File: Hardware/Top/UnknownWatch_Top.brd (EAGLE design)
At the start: 38 x 38 mm, 54 parts, among them SW1 SWITCH.MOM, SW6 SWITCH.MOM, U2 NRF52832_MODULE_MDBT42, U4 PCF8523, U5 PHOTOTRANSISTOR

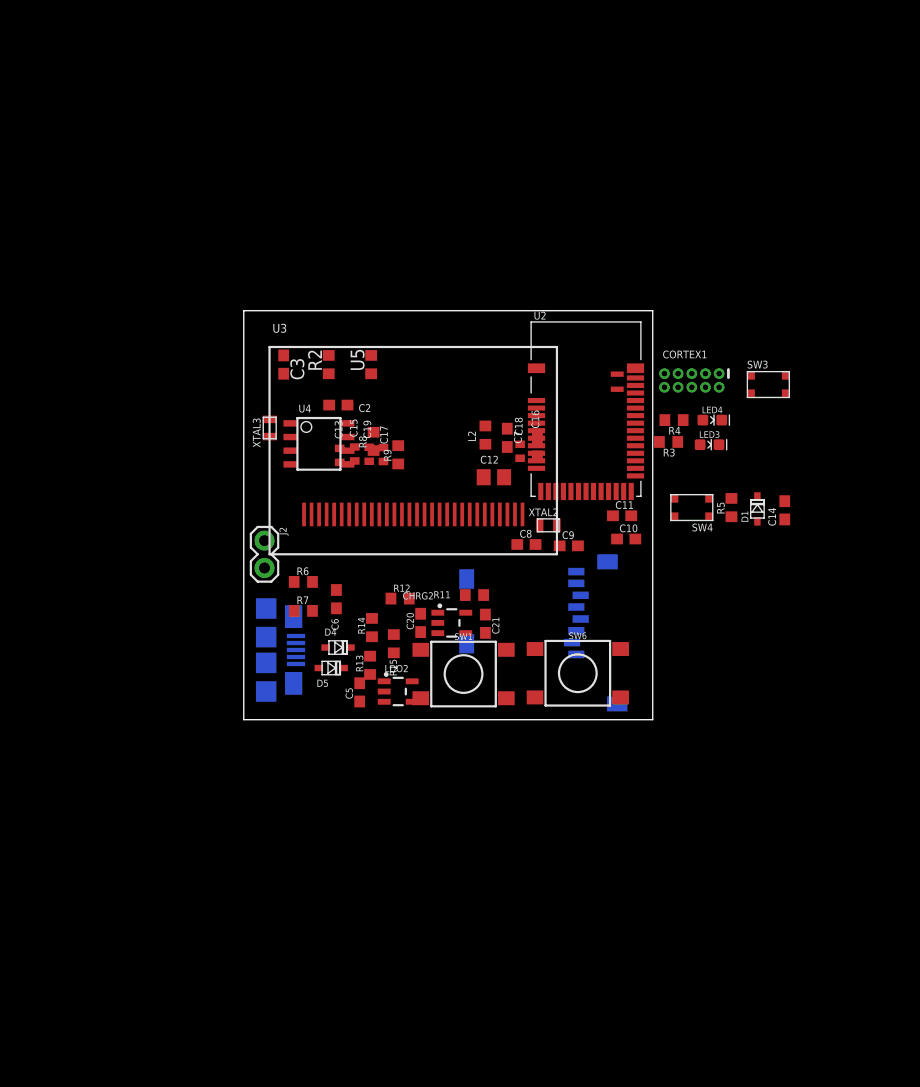
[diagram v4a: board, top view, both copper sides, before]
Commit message: Added connections from bottom to top board and other various changes.
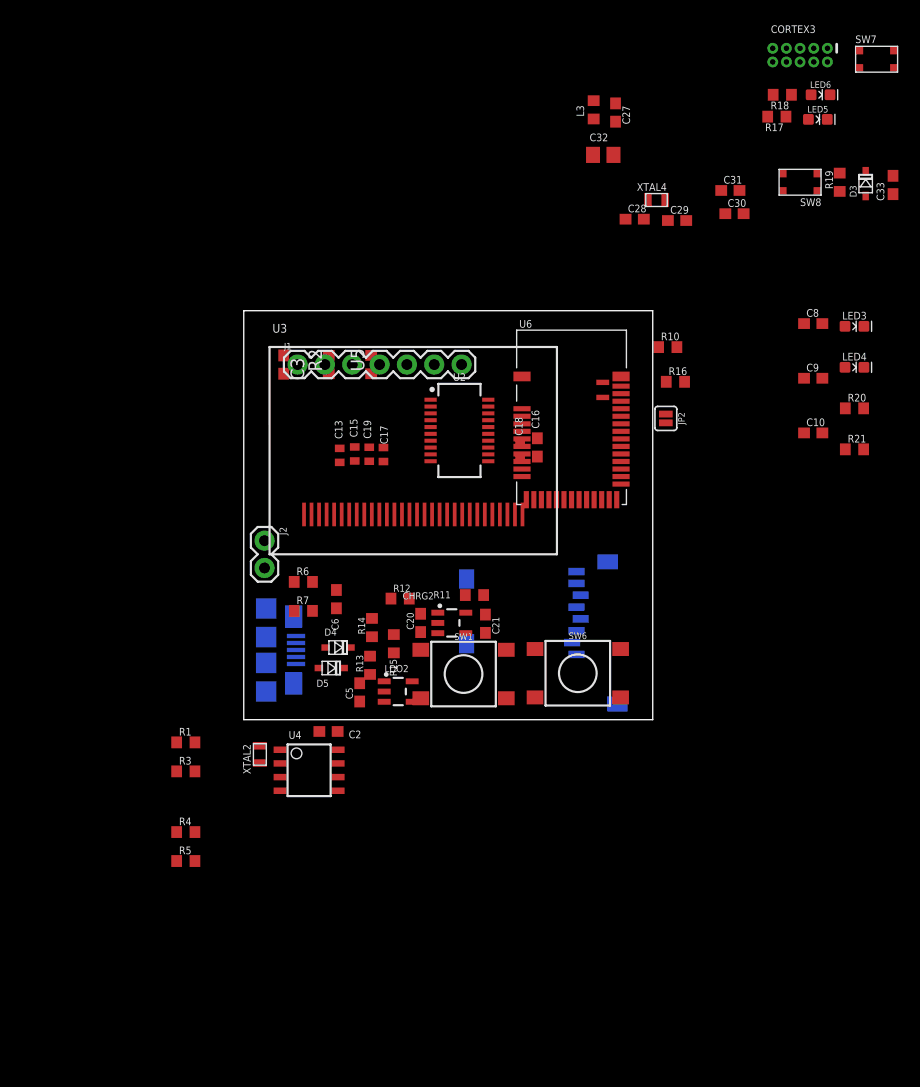
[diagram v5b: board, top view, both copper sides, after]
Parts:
- removed C11: 300p, LinnesLab-Passives:C0603
- removed C12: 10u, LinnesLab-Passives:C0805
- removed C14: 100n, LinnesLab-Passives:C0603
- removed C7: 1u, LinnesLab-Passives:C0603
- removed CORTEX1: CORTEX_DEBUG_PTH, LinnesLab-Connectors:2X5-PTH-1.27MM
- removed D1: (no value), LinnesLab-DiscreteSemi:USC
- removed L2: 10u, LinnesLab-Passives:L0603
- removed R8, R9: 10k, LinnesLab-Passives:R0603
- removed SW3, SW4: (no value), LinnesLab-Switches:BUTTON-GULLWING
- removed XTAL3: 32.7680kHz, LinnesLab-Clocks:2-SMD.NOLEAD.2.0MMTO1.2MM
- added C27: 1u, LinnesLab-Passives:C0603
- added C28, C29: (no value), LinnesLab-Passives:C0603
- added C30, C31: 300p, LinnesLab-Passives:C0603
- added C32: 10u, LinnesLab-Passives:C0805
- added C33: 100n, LinnesLab-Passives:C0603
- added CORTEX3: CORTEX_DEBUG_PTH, LinnesLab-Connectors:2X5-PTH-1.27MM
- added D3: (no value), LinnesLab-DiscreteSemi:USC
- added J1: (no value), LinnesLab-Connectors:1X07
- added JP2: (no value), LinnesLab-Switches:SMT-JUMPER_2_NO_SILK
- added L3: 10u, LinnesLab-Passives:L0603
- added LED5: RED, LinnesLab-LED:LED-0603
- added LED6: BLUE, LinnesLab-LED:LED-0603
- added R1: 0, LinnesLab-Passives:R0603
- added R10, R16: 27, LinnesLab-Passives:R0603
- added R17, R18, R20, R21: 1k, LinnesLab-Passives:R0603
- added R19: 10k, LinnesLab-Passives:R0603
- added SW7, SW8: (no value), LinnesLab-Switches:BUTTON-GULLWING
- added U6: NRF52832_MODULE_MDBT42, LinnesLab-Microcontrollers:BLE_MODULE_RAYTAC_MDBT42
- added XTAL4: 32.768kHz, LinnesLab-Clocks:2-SMD.NOLEAD.2.0MMTO1.2MM
- C10: value 300p -> 47p
- C8: value (none) -> 100n
- C9: value (none) -> 47p
- LED4: value BLUE -> YELLOW
- R3: value 1k -> 0
- R4: value 1k -> 10K
- R5: value 10k -> 10K
- U2: value NRF52832_MODULE_MDBT42 -> FT231XS; device LinnesLab-Microcontrollers:BLE_MODULE_RAYTAC_MDBT42 -> LinnesLab-DigitalIC:SSOP20_L
- XTAL2: value 32.768kHz -> 32.7680kHz
- moved R5 60.4 mm to (-5.38, -13.1), turned to 0 degrees
- moved R4 59.4 mm to (-5.38, -10.4), turned to 0 degrees
- moved R3 54.3 mm to (-5.38, -4.80), turned to 0 degrees
- moved XTAL2 34.2 mm to (1.50, -3.23), turned to 90 degrees
- moved C8 33.6 mm to (52.9, 36.8)
- moved C2 30.3 mm to (7.87, -1.09)
- moved U4 30.3 mm to (6.07, -4.70)
- moved C9 27.5 mm to (52.9, 31.7)
- moved C10 20.0 mm to (52.9, 26.6)
- moved LED3 17.4 mm to (56.7, 36.6)
- moved LED4 14.1 mm to (56.7, 32.7)
- moved U2 11.9 mm to (20.0, 26.9), turned to 270 degrees
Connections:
- removed net N$10: LED4.A, R4.1
- removed net N$19: U4.2, XTAL3.P$1
- removed net N$20: U4.1, XTAL3.P$2
- removed net N$4: C8.2, U2.13, XTAL2.P$1
- removed net RXD: U2.21
- removed net TXD: U2.19
- new net !CTS: JP2.2, U2.9
- new net FT3V3: U2.13
- new net N$16: LED4.C, R21.2
- new net N$26: C28.2, U6.13, XTAL4.P$1
- new net N$27: C29.1, U6.14, XTAL4.P$2
- new net N$28: LED5.A, R17.1
- new net N$29: LED6.A, R18.1
- new net N$30: L3.1, U6.10
- new net N$31: C27.1, L3.2, U6.9
- new net N$32: CORTEX3.8
- new net RXD.FT: R3.1, U2.4
- new net RXD.NRF: R1.2, U6.21
- new net RXLED: R20.1, U2.17
- new net TXD.FT: R1.1, U2.20
- new net TXD.NRF: R3.2, U6.19
- new net TXLED: R21.1, U2.10
- net 3.3V: now also C32.2, C8.2, CORTEX3.1, D3.-, LED3.A, LED4.A, R19.2, R4.2, U2.14, U2.3, U6.11; no longer C12.2, CORTEX1.1, D1.-, R8.2, R9.2, U2.11
- net DFU: now also SW7.3, U6.34; no longer SW3.3, U2.34
- net DTR: now also C33.1, U2.1; no longer C14.1
- net FRST: now also U6.38; no longer U2.38
- net GND: now also C10.1, C27.2, C28.1, C29.2, C30.2, C31.2, C32.1, CORTEX3.3, CORTEX3.5, CORTEX3.7, CORTEX3.9, JP2.1, LED5.C, LED6.C, SW7.1, SW8.3, U2.16, U2.6, U6.1, U6.12, U6.24, U6.39; no longer C10.2, C11.2, C12.1, C7.2, CORTEX1.3, CORTEX1.5, CORTEX1.7, CORTEX1.9, LED3.C, LED4.C, SW3.1, SW4.3, U2.1, U2.12, U2.24, U2.39
- net LED1: now also R17.2, U6.31; no longer R3.2, U2.31
- net LED2: now also R18.2, U6.33; no longer R4.2, U2.33
- net MISO: now also U6.28; no longer U2.28
- net MOSI: now also U6.27; no longer U2.27
- net N$11: now also R10.2, U2.12; no longer L2.1, U2.10
- net N$12: now also R16.2, U2.11; no longer C7.1, L2.2, U2.9
- net N$14: now also LED3.C, R20.2; no longer CORTEX1.8
- net N$6: now also U4.2, XTAL2.P$1; no longer C9.1, U2.14, XTAL2.P$2
- net N$9: now also U4.1, XTAL2.P$2; no longer LED3.A, R3.1
- net P0.09/NFC1: now also C31.1, U6.22; no longer C11.1, U2.22
- net P0.10/NFC2: now also C30.1, U6.23; no longer C10.1, U2.23
- net RESET: now also C33.2, CORTEX3.10, D3.+, R19.1, SW8.1, U6.35; no longer C14.2, CORTEX1.10, D1.+, R5.1, SW4.1, U2.35
- net SCK: now also U6.26; no longer U2.26
- net SCL: now also R5.1, U6.3; no longer R8.1, U2.3
- net SDA: now also R4.1, U6.2; no longer R9.1, U2.2
- net SWCLK: now also CORTEX3.4, U6.36; no longer CORTEX1.4, U2.36
- net SWDIO: now also CORTEX3.2, U6.37; no longer CORTEX1.2, U2.37
- net SWO: now also CORTEX3.6, U6.32; no longer CORTEX1.6, U2.32
- net USB+: now also C9.1, R16.1
- net USB-: now also C10.2, R10.1
- net V_USB: now also U2.15

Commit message: Made all changes associated wih take 002
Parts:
- renumbered SW1 to SW2
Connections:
- removed net BATT: R13.1, R14.2
- removed net CD1: SD2.CD1
- removed net CHRG.STAT: CHRG2.1, R12.1
- removed net CS.OLED: U3.13
- removed net DC.OLED: U3.15
- removed net RESET.OLED: U3.14
- removed net SD.CS: SD2.2
- removed net SW1: SW2.A1, SW6.A1
- new net A4/BATT: R13.1, R14.2, U6.5
- new net A6/TIA: U6.7
- new net A7/PPG: U6.8
- new net D11/SW1: SW6.A1, U6.25
- new net D15/SW2: SW2.A1, U6.29
- new net D16/CS.OLED: U3.13, U6.30
- new net D27/CHRG.STATUS: CHRG2.1, R12.1, U6.4
- new net D29/LED.CTRL: U6.6
- new net D3/RESET.OLED: U3.14, U6.16
- new net D4/DC.OLED: U3.15, U6.17
- new net D5/CD1: SD2.CD1, U6.18
- new net D7/SD.CS: SD2.2, U6.20
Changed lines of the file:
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@@
 <attribute name="VALUE" x="31.0388" y="1.143" size="0.6096" layer="27" ratio="20" align="top-center"/>
 </element>
-<element name="SW1" library="LinnesLab-Switches" package="TACTILE_SWITCH_SMD_6.2MM_TALL" value="SWITCH.MOM" x="20.4216" y="4.2418" smashed="yes">
+<element name="SW2" library="LinnesLab-Switches" package="TACTILE_SWITCH_SMD_6.2MM_TALL" value="SWITCH.MOM" x="20.4216" y="4.2418" smashed="yes">
 <attribute name="NAME" x="20.4216" y="7.4168" size="0.6096" layer="25" ratio="20" align="bottom-center"/>
 <attribute name="VALUE" x="20.4216" y="1.0668" size="0.6096" layer="27" ratio="20" align="top-center"/>
@@
 <contactref element="SW6" pad="B1"/>
 <contactref element="SW6" pad="B2"/>
-<contactref element="SW1" pad="B1"/>
-<contactref element="SW1" pad="B2"/>
+<contactref element="SW2" pad="B1"/>
+<contactref element="SW2" pad="B2"/>
 <contactref element="C27" pad="2"/>
 <contactref element="C28" pad="1"/>
@@
 <contactref element="U6" pad="38"/>
 </signal>
-<signal name="DC.OLED">
-<contactref element="U3" pad="15"/>
-</signal>
-<signal name="RESET.OLED">
-<contactref element="U3" pad="14"/>
-</signal>
 <signal name="N$1">
 <contactref element="U3" pad="11"/>
@@
 <wire x1="23.798" y1="19.0692" x2="25.6794" y2="25.5928" width="0" layer="19" extent="1-1"/>
 </signal>
-<signal name="CS.OLED">
-<contactref element="U3" pad="13"/>
-</signal>
 <signal name="CD2">
 <contactref element="SD2" pad="CD2"/>
-</signal>
-<signal name="CD1">
-<contactref element="SD2" pad="CD1"/>
-</signal>
-<signal name="SD.CS">
-<contactref element="SD2" pad="2"/>
 </signal>
 <signal name="N$17">
@@
 <wire x1="4.8578" y1="5.177" x2="6.978" y2="4.8006" width="0" layer="19" extent="1-16"/>
 </signal>
-<signal name="CHRG.STAT">
-<contactref element="R12" pad="1"/>
-<contactref element="CHRG2" pad="1"/>
-<wire x1="13.6788" y1="11.2522" x2="18.0293" y2="9.9416" width="0" layer="19" extent="1-1"/>
-</signal>
 <signal name="USB-">
 <contactref element="USB2" pad="2"/>
@@
 <wire x1="39.2566" y1="31.3944" x2="52.0582" y2="31.7246" width="0" layer="19" extent="1-1"/>
 <wire x1="4.8578" y1="6.477" x2="39.2566" y2="31.3944" width="0" layer="19" extent="1-16"/>
-</signal>
-<signal name="BATT">
-<contactref element="R13" pad="1"/>
-<contactref element="R14" pad="2"/>
-<wire x1="11.9126" y1="9.4098" x2="11.7348" y2="4.2046" width="0" layer="19" extent="1-1"/>
 </signal>
 <signal name="VIN">
@@
 <wire x1="3.7084" y1="33.8446" x2="7.8994" y2="33.8446" width="0" layer="19" extent="1-1"/>
 </signal>
-<signal name="SW1">
-<contactref element="SW6" pad="A1"/>
-<contactref element="SW1" pad="A1"/>
-<wire x1="16.4466" y1="1.9918" x2="27.0638" y2="2.068" width="0" layer="19" extent="1-1"/>
-</signal>
 <signal name="N$26">
 <contactref element="C28" pad="2"/>
@@
 <contactref element="U4" pad="3"/>
 </signal>
+<signal name="D27/CHRG.STATUS">
+<contactref element="U6" pad="4"/>
+<contactref element="R12" pad="1"/>
+<contactref element="CHRG2" pad="1"/>
+<wire x1="18.0293" y1="9.9416" x2="25.8546" y2="27.4924" width="0" layer="19" extent="1-1"/>
+<wire x1="13.6788" y1="11.2522" x2="18.0293" y2="9.9416" width="0" layer="19" extent="1-1"/>
+</signal>
+<signal name="A4/BATT">
+<contactref element="U6" pad="5"/>
+<contactref element="R13" pad="1"/>
+<contactref element="R14" pad="2"/>
+<wire x1="11.9126" y1="9.4098" x2="25.8546" y2="26.7924" width="0" layer="19" extent="1-1"/>
+<wire x1="11.7348" y1="4.2046" x2="11.9126" y2="9.4098" width="0" layer="19" extent="1-1"/>
+</signal>
+<signal name="D7/SD.CS">
+<contactref element="U6" pad="20"/>
+<contactref element="SD2" pad="2"/>
+<wire x1="30.5092" y1="7.1622" x2="31.8546" y2="20.4424" width="0" layer="19" extent="1-16"/>
+</signal>
+<signal name="D5/CD1">
+<contactref element="U6" pad="18"/>
+<contactref element="SD2" pad="CD1"/>
+<wire x1="20.7092" y1="13.0622" x2="30.4546" y2="20.4424" width="0" layer="19" extent="1-16"/>
+</signal>
+<signal name="D11/SW1">
+<contactref element="U6" pad="25"/>
+<contactref element="SW6" pad="A1"/>
+<wire x1="27.0638" y1="2.068" x2="35.0546" y2="21.8924" width="0" layer="19" extent="1-1"/>
+</signal>
+<signal name="D15/SW2">
+<contactref element="U6" pad="29"/>
+<contactref element="SW2" pad="A1"/>
+<wire x1="16.4466" y1="1.9918" x2="35.0546" y2="24.6924" width="0" layer="19" extent="1-1"/>
+</signal>
+<signal name="D16/CS.OLED">
+<contactref element="U6" pad="30"/>
+<contactref element="U3" pad="13"/>
+<wire x1="13.998" y1="19.0692" x2="35.0546" y2="25.3924" width="0" layer="19" extent="1-1"/>
+</signal>
+<signal name="D4/DC.OLED">
+<contactref element="U6" pad="17"/>
+<contactref element="U3" pad="15"/>
+<wire x1="15.398" y1="19.0692" x2="29.7546" y2="20.4424" width="0" layer="19" extent="1-1"/>
+</signal>
+<signal name="D3/RESET.OLED">
+<contactref element="U6" pad="16"/>
+<contactref element="U3" pad="14"/>
+<wire x1="14.698" y1="19.0692" x2="29.0546" y2="20.4424" width="0" layer="19" extent="1-1"/>
+</signal>
+<signal name="D29/LED.CTRL">
+<contactref element="U6" pad="6"/>
+</signal>
+<signal name="A6/TIA">
+<contactref element="U6" pad="7"/>
+</signal>
+<signal name="A7/PPG">
+<contactref element="U6" pad="8"/>
+</signal>
 </signals>

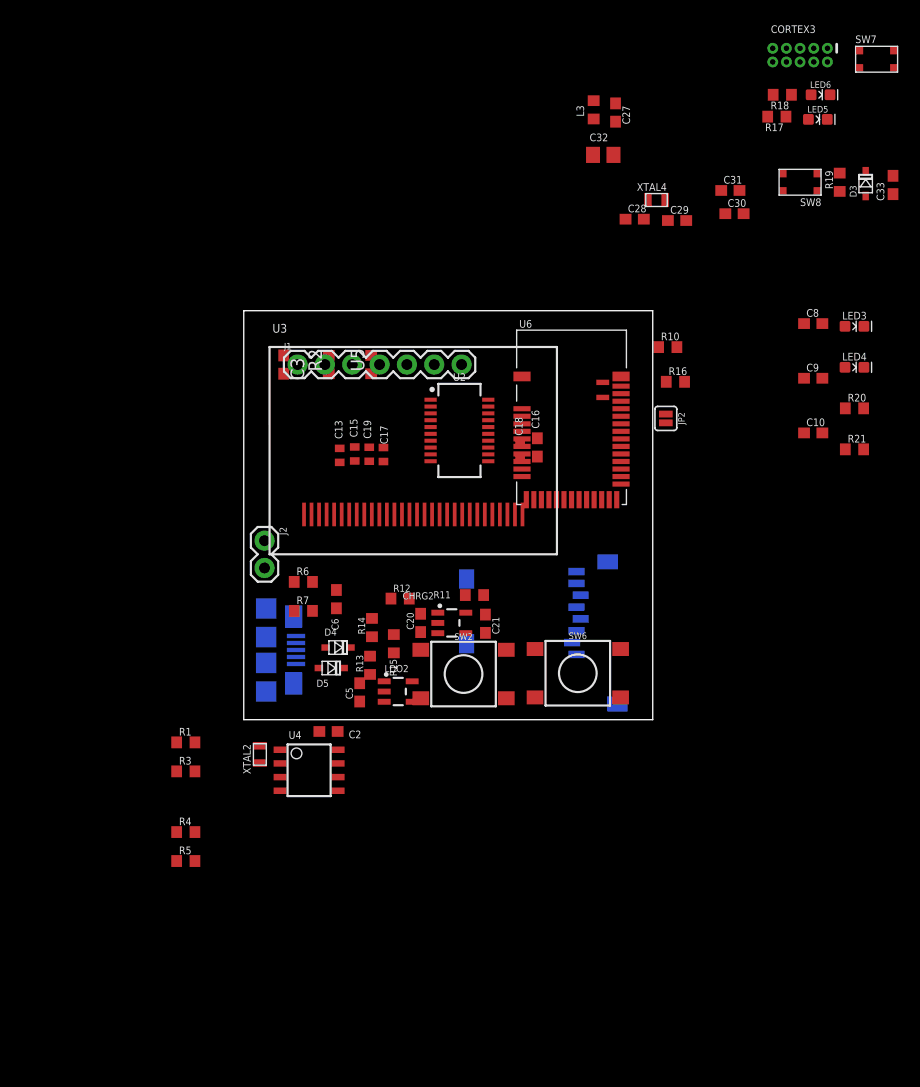
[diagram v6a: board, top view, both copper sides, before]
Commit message: Began routing top board.
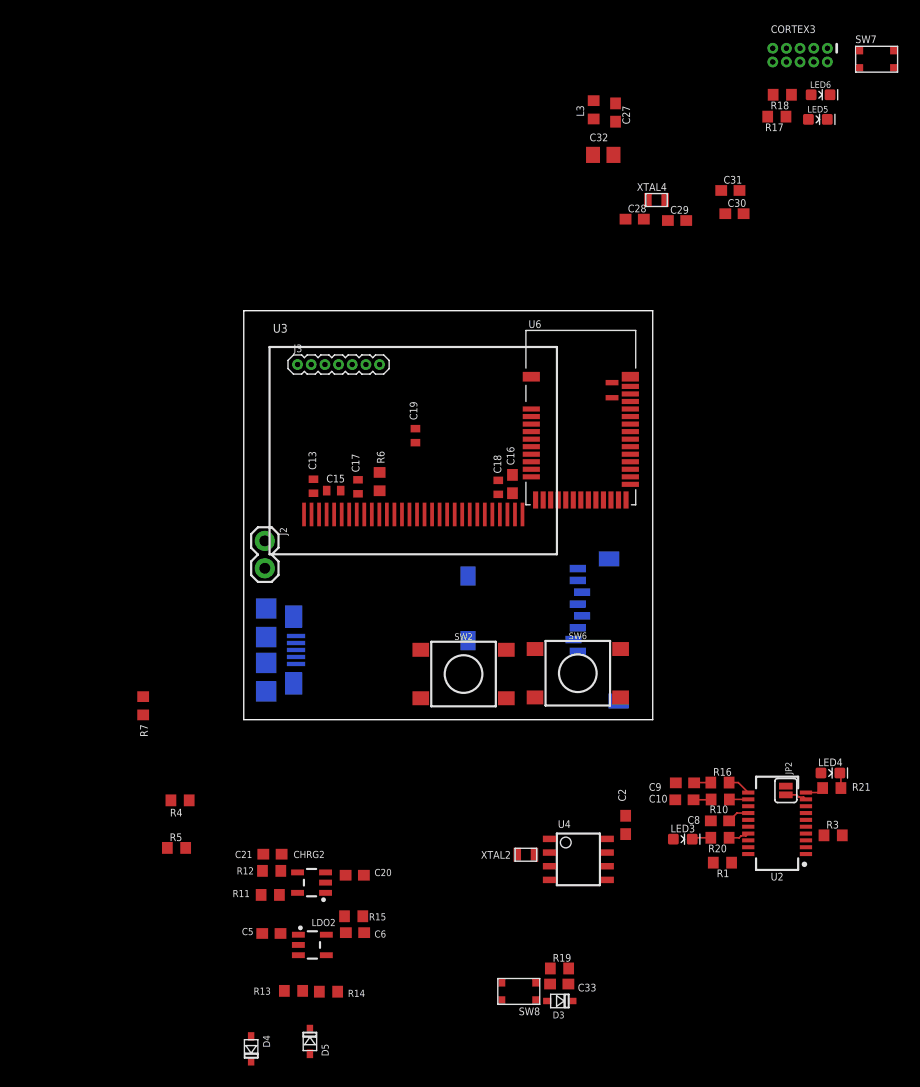
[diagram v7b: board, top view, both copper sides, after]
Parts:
- removed C3: 2.2u, LinnesLab-Passives:C0603
- removed J1: (no value), LinnesLab-Connectors:1X07
- removed R2: 10k, LinnesLab-Passives:R0603
- removed U5: PHOTOTRANSISTOR, LinnesLab-Sensors:R0603
- added J3: (no value), LinnesLab-Connectors:1X07_1.27MM
- moved D3 81.1 mm to (29.4, -26.1), turned to 0 degrees
- moved C33 80.5 mm to (29.3, -24.6), turned to 180 degrees
- moved SW8 79.6 mm to (25.6, -25.2)
- moved R19 77.6 mm to (29.3, -23.1), turned to 0 degrees
- moved R3 60.4 mm to (54.8, -10.7)
- moved R1 51.1 mm to (44.5, -13.3), turned to 180 degrees
- moved LED3 50.2 mm to (40.8, -11.1)
- moved C8 47.0 mm to (44.2, -9.40)
- moved U2 46.9 mm to (49.6, -9.63), turned to 90 degrees
- moved R10 42.3 mm to (44.3, -7.42)
- moved R20 41.8 mm to (44.2, -11.0), turned to 180 degrees
- moved C9 39.4 mm to (41.0, -5.87), turned to 180 degrees
- moved D4 38.2 mm to (0.69, -30.6), turned to 270 degrees
- moved LED4 37.8 mm to (54.5, -4.95)
- moved R16 37.5 mm to (44.2, -5.84)
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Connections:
- removed net OUTPUT: C3.1, R2.2, U5.2
- net 3.3V: now also J3.4; no longer U5.1
- net A6/TIA: now also J3.6
- net A7/PPG: now also J3.7
- net D29/LED.CTRL: now also J3.5
- net GND: now also J3.3; no longer C3.2, R2.1
- net SCL: now also J3.2
- net SDA: now also J3.1
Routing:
- net 3.3V: track 0.00 -> 2.36 mm
- net N$12: track 0.00 -> 2.16 mm
- net !CTS: track 0.00 -> 2.04 mm
- net RXLED: track 0.00 -> 1.94 mm
- net N$14: track 0.00 -> 1.78 mm
- net N$11: track 0.00 -> 1.76 mm
- net TXLED: track 0.00 -> 1.72 mm
- net USB-: track 0.00 -> 1.64 mm
- net USB+: track 0.00 -> 1.56 mm
- net N$16: track 0.00 -> 1.44 mm

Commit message: Complted all routing of top board associated with take 4.
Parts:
- removed C30, C31: 300p, LinnesLab-Passives:C0603
- removed R15: 100k, LinnesLab-Passives:R0603
- moved C8 66.3 mm to (-17.2, 15.5)
- moved LED4 66.3 mm to (-6.93, 19.9)
- moved R1 66.3 mm to (-17.0, 11.6)
- moved R10 66.3 mm to (-17.2, 17.5)
- moved R16 66.3 mm to (-17.2, 19.1)
- moved R20 66.3 mm to (-17.2, 13.9)
- moved R21 66.3 mm to (-6.81, 18.5)
- moved R3 66.3 mm to (-6.68, 14.1)
- moved U2 66.3 mm to (-11.9, 15.3)
- moved JP2 66.2 mm to (-11.1, 18.0)
- moved LED3 65.1 mm to (-19.6, 13.1), turned to 90 degrees
- moved C10 65.0 mm to (-19.4, 16.7), turned to 90 degrees
- moved C9 64.0 mm to (-17.3, 20.5), turned to 0 degrees
- moved R7 40.8 mm to (27.8, 18.1), turned to 0 degrees
- moved D4 34.9 mm to (7.77, 3.61), flipped to the bottom
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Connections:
- net 3.3V: no longer R15.2
- net GND: no longer C30.2, C31.2, R15.1, SW2.B2, SW6.B2
- net P0.09/NFC1: no longer C31.1
- net P0.10/NFC2: no longer C30.1
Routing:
- net GND: track 0.00 -> 42.4 mm, vias 0 -> 11
- net VLIPO: track 0.00 -> 14.1 mm
- net VIN: track 0.00 -> 7.64 mm
- net 3.3V: track 2.36 -> 8.52 mm, vias 0 -> 1
- net N$2: track 0.00 -> 6.11 mm
- net N$15: track 0.00 -> 4.54 mm
- net N$13: track 0.00 -> 4.53 mm
- net N$31: track 0.00 -> 4.26 mm
- net N$3: track 0.00 -> 4.08 mm
- net N$8: track 0.00 -> 2.47 mm
- net N$30: track 0.00 -> 2.36 mm
- net N$1: track 0.00 -> 2.23 mm
- net N$7: track 0.00 -> 2.22 mm
- net N$5: track 0.00 -> 2.19 mm
- net TXD.FT: track 0.00 -> 1.88 mm
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- added copper zone on layer 1, net 3.3V
- added copper zone on layer 16, net GND
